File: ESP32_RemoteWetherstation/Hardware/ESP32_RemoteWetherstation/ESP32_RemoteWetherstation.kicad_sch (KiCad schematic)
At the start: 5 parts, among them J301 BOOT, J302 UART, U301 ESP32-WROOM-32E

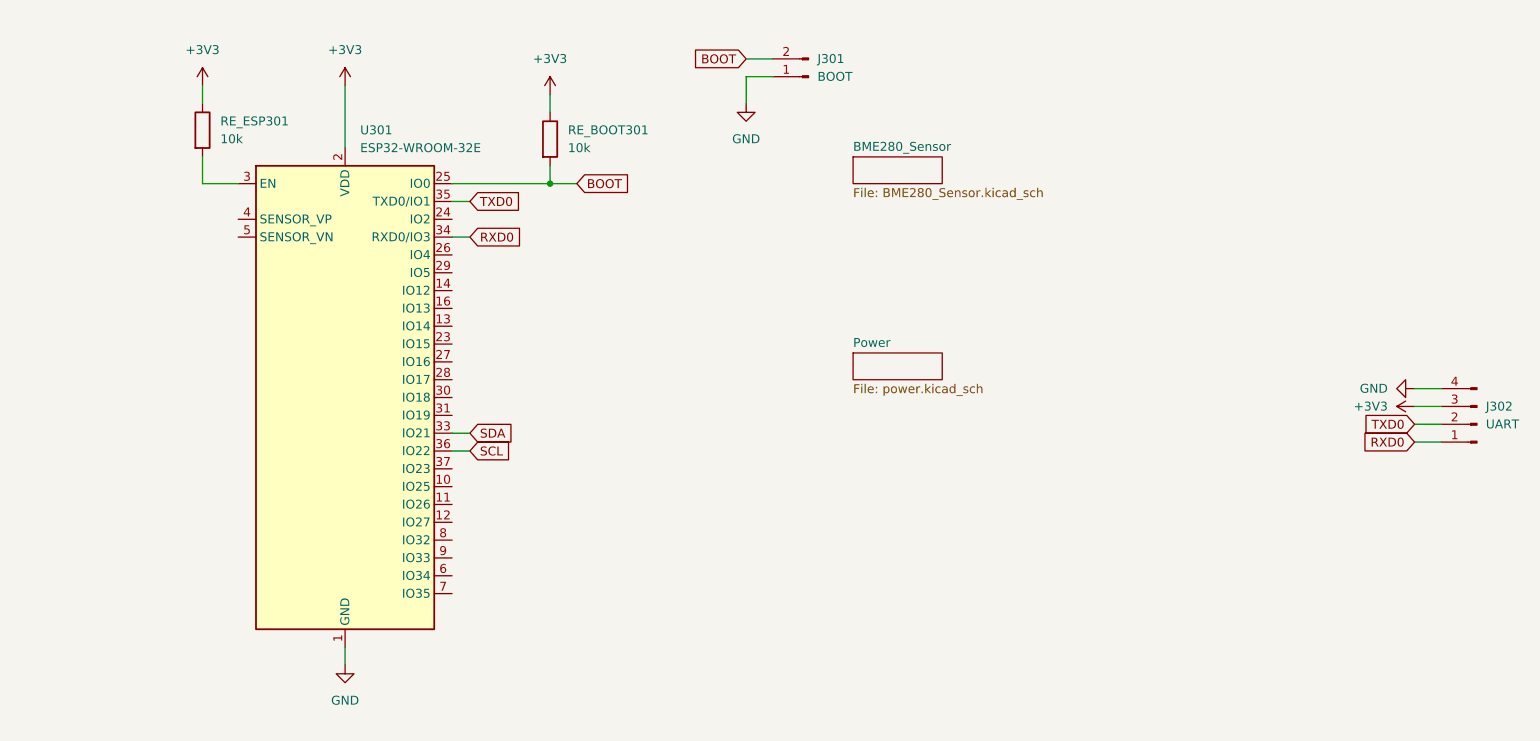
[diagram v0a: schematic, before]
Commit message: added IO, changed LDO
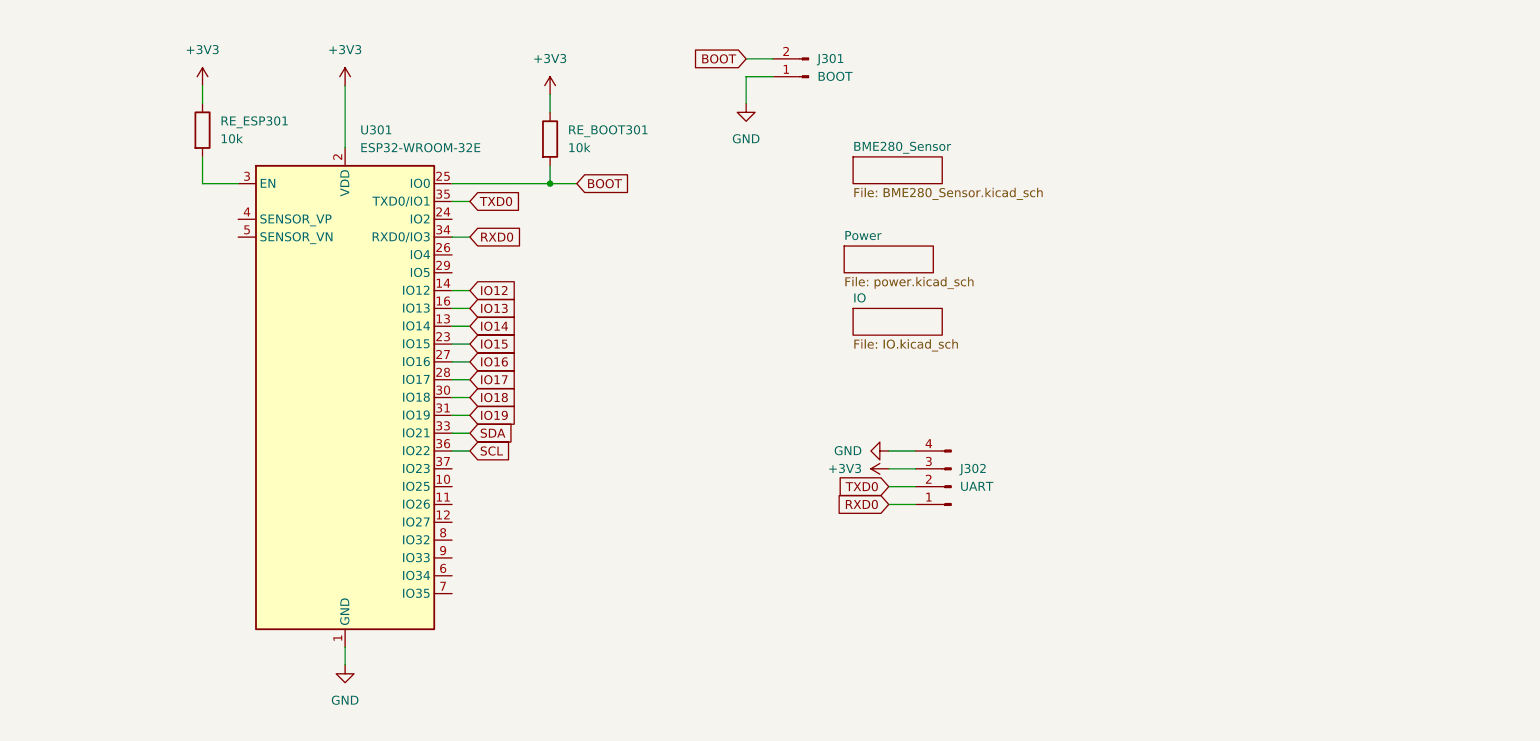
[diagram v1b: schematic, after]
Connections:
- net IO14: now reaches U301.13 (IO14)
- net IO12: now reaches U301.14 (IO12)
- net IO13: now reaches U301.16 (IO13)
- net IO15: now reaches U301.23 (IO15)
- net IO16: now reaches U301.27 (IO16)
- net IO17: now reaches U301.28 (IO17)
- net IO18: now reaches U301.30 (IO18)
- net IO19: now reaches U301.31 (IO19)
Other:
- added sheet IO (IO.kicad_sch)
- moved on the sheet: J302

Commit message: edited schematic looks
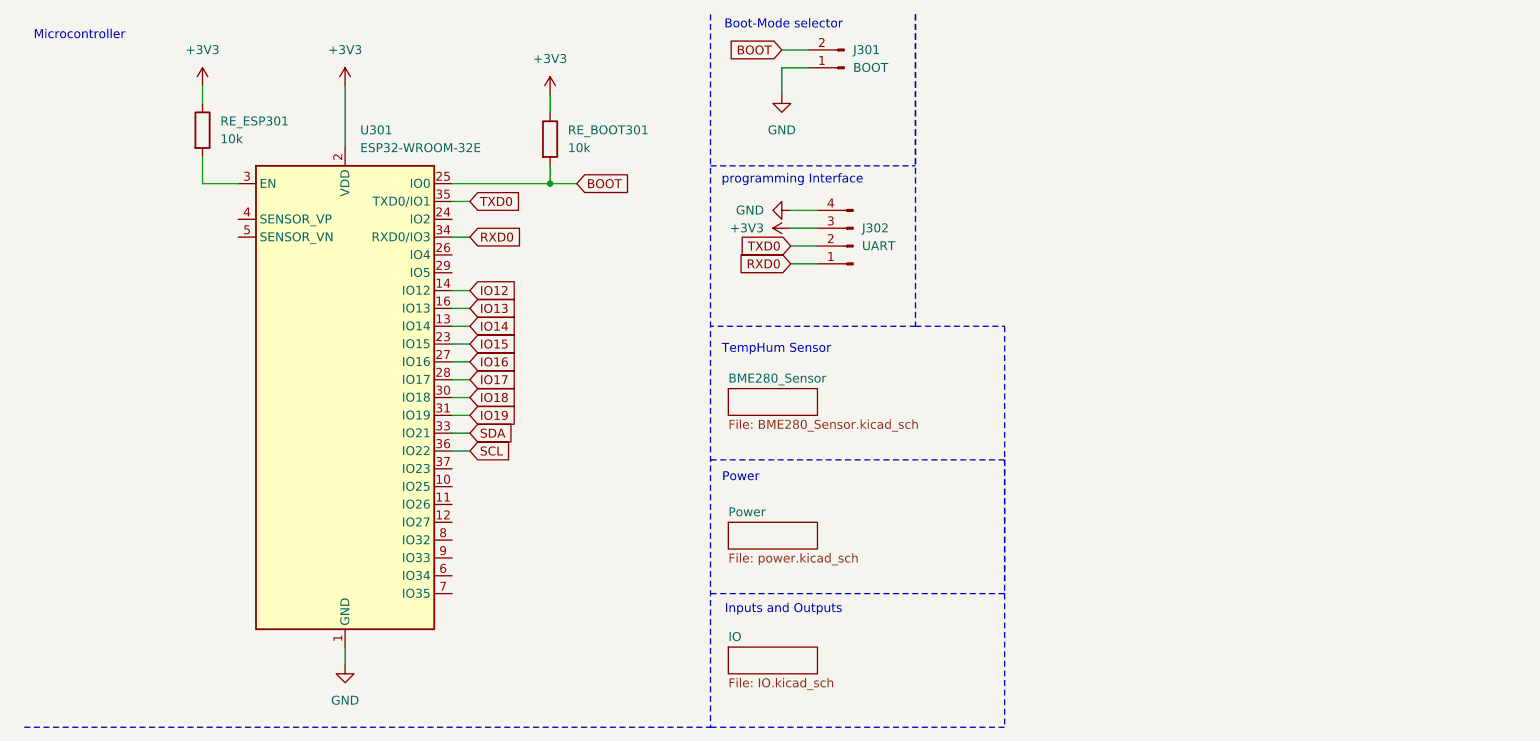
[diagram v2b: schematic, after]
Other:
- note added: "Boot-Mode selector"
- note added: "Inputs and Outputs"
- note added: "Microcontroller"
- note added: "Power"
- note added: "TempHum Sensor"
- note added: "programming Interface"
- moved on the sheet: J301, J302

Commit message: changed MCU
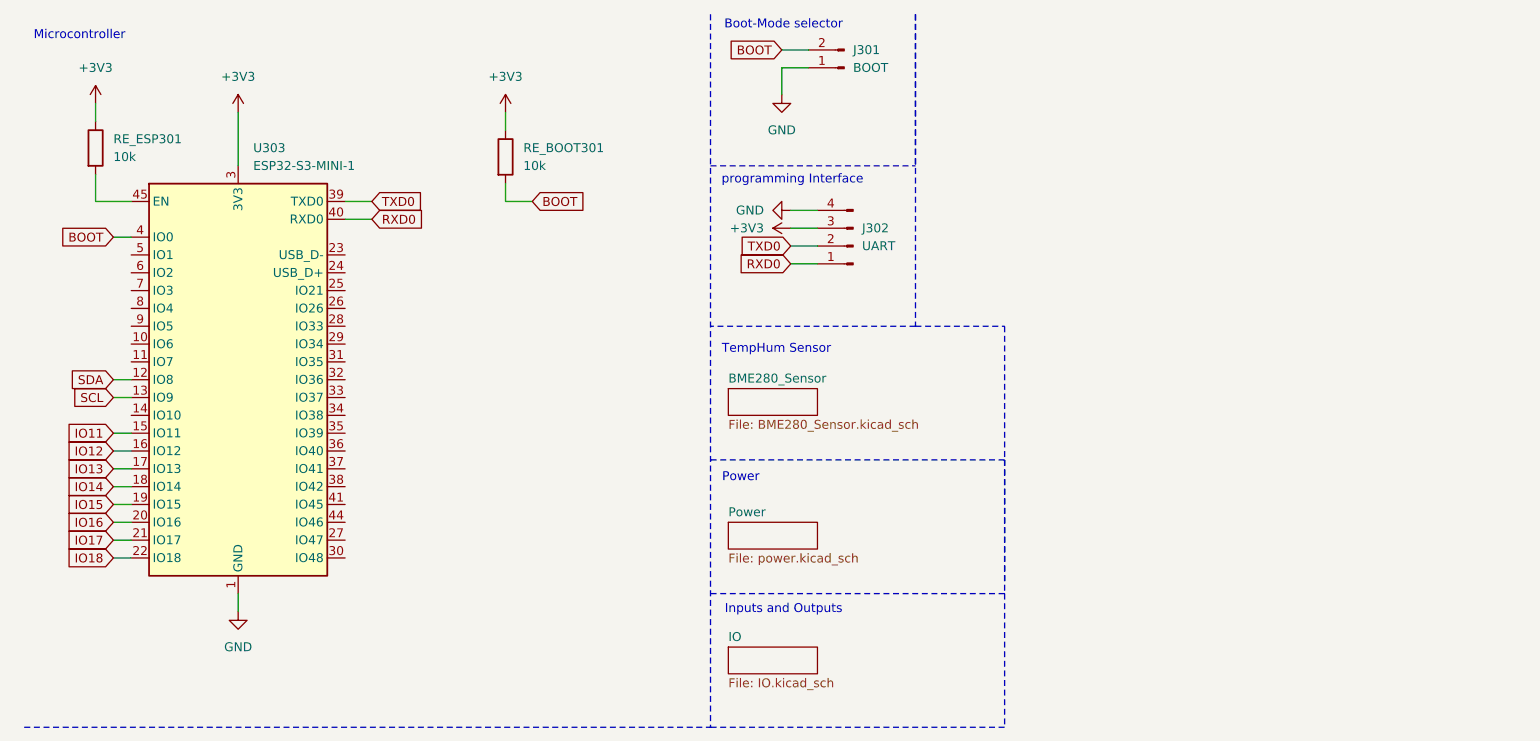
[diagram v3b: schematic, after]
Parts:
- removed U301: ESP32-WROOM-32E, RF_Module:ESP32-WROOM-32D, symbol RF_Module:ESP32-WROOM-32E
- added U303: ESP32-S3-MINI-1, RF_Module:ESP32-S2-MINI-1, symbol RF_Module:ESP32-S3-MINI-1
- RE_BOOT301, RE_ESP301: footprint Resistor_SMD:R_0603_1608Metric -> Resistor_SMD:R_0402_1005Metric
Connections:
- net +3V3: now also U303.3 (3V3)
- net BOOT: now also U303.4 (IO0)
- net GND: now also U303.1 (GND), U303.2 (GND), U303.42 (GND), U303.43 (GND), U303.46 (GND), U303.47 (GND), U303.48 (GND), U303.49 (GND), U303.50 (GND), U303.51 (GND), U303.52 (GND), U303.53 (GND), U303.54 (GND), U303.55 (GND), U303.56 (GND), U303.57 (GND), U303.58 (GND), U303.59 (GND), U303.60 (GND), U303.61 (GND), U303.62 (GND), U303.63 (GND), U303.64 (GND), U303.65 (GND)
- net IO12: now also U303.16 (IO12)
- net IO13: now also U303.17 (IO13)
- net IO14: now also U303.18 (IO14)
- net IO15: now also U303.19 (IO15)
- net IO16: now also U303.20 (IO16)
- net IO17: now also U303.21 (IO17)
- net IO18: now also U303.22 (IO18)
- net RXD0: now also U303.40 (RXD0)
- net SCL: now also U303.13 (IO9)
- net SDA: now also U303.12 (IO8)
- net TXD0: now also U303.39 (TXD0)
- net at RE_ESP301.2: now also U303.45 (EN)
- new net IO11: U303.15 (IO11)
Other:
- moved on the sheet: RE_ESP301

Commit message: stitching/PowerModule
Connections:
- net RXD0: now also J302.2 (Pin_2); no longer J302.1 (Pin_1)
- net TXD0: now also J302.1 (Pin_1); no longer J302.2 (Pin_2)
